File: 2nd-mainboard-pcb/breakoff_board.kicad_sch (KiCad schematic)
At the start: 28 parts, among them J13 ISP, J14 Spannungsmessung, J7 Quartz

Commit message: added libraries
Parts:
- added TP20: Quartz_2, symbol Connector:TestPoint
- TP1: value TestPoint -> Quartz_1
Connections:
- net Quartz_1: now also TP1.1
- net Quartz_2: now also TP20.1
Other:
- note added: "ADC-Messungen"
- note added: "Quartzmessung: Oszilloskop-Testpoints"
- note removed: "JTAG und ADC-Messungen Joint Test Action Group: standardisierte Schnittstelle für das Debugging und Testen von Mikrocontrollern"
- note removed: "Quartzmessung"
- note removed: "TDI (Test Data In) PC2 TDO (Test Data Out) PC3 TMS (Test Mode Select) PC4 TCK (Test Clock) PC5"
- moved on the sheet: J7, R14, R15, R16, TP1, TP14, TP15, TP16, TP17, TP7, TP8

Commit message: finished stacked design, annotaded
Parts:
- removed J14: Spannungsmessung, symbol Connector:Conn_01x05_Socket
- removed R16: 0.1, symbol Device:R
- removed TP16: I_Sense_12V_P, symbol Connector:TestPoint_Probe
- added J17: Spannungsmessung, symbol Connector:Conn_01x06_Socket
- added R23, R24: 0.1, symbol Device:R
- added TP13: I_Sense_12V_P, symbol Connector:TestPoint_Probe
- added TP14: I_Sense_12V_N, symbol Connector:TestPoint_Probe
- added TP7: I_Sense_5V_POW_P, symbol Connector:TestPoint_Probe
- added TP8: I_Sense_5V_POW_N, symbol Connector:TestPoint_Probe
- added TP9: I_Sense_5V, symbol Connector:TestPoint_2Pole
- TP17: value I_Sense_12V_N -> Netzteil_Test; footprint (none) -> TestPoint:TestPoint_Pad_D3.0mm
- TP5: renamed from TP14; value I_Sense_5V_P -> I_Sense_5V_USBC_P
- TP6: renamed from TP15; value I_Sense_5V_N -> I_Sense_5V_USBC_N
- renumbered D7 to D6, J13 to J18, J7 to J19, R17 to R20, R14 to R21, R15 to R22, R19 to R25, TP7 to TP1, TP19 to TP10, TP4 to TP11, TP2 to TP12, TP3 to TP15, TP5 to TP16, TP9 to TP18, TP12 to TP19, TP8 to TP2, TP13 to TP20, TP1 to TP21, TP11 to TP22, TP20 to TP23, TP10 to TP24, TP18 to TP3, TP6 to TP4
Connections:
- net +12V: now also J17.4 (Pin_4), R24.1, TP13.1
- net +3V3: now also J17.1 (Pin_1)
- net +5V: now also J17.2 (Pin_2), TP9.1; no longer R22.1, TP5.1
- net GND: now also J17.3 (Pin_3), R23.2, R24.2, TP14.1, TP8.1, TP9.2; no longer TP17.1
- net GND2: now also J17.6 (Pin_6)
- new net +24V: J17.5 (Pin_5), TP17.1
- new net +5V_POW: R23.1, TP7.1
- new net +5V_USBC: R22.1, TP5.1
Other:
- moved on the sheet: D6, J18, J19, R20, R21, R22, R25, TP1, TP10, TP11, TP12, TP15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

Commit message: alle bauteile hinzugefügt
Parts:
- removed J17: Spannungsmessung, symbol Connector:Conn_01x06_Socket
- removed J18: ISP, symbol Connector_Generic:Conn_02x03_Odd_Even
- added J21: ISP, Imported_Component_Footprints:FTSH-103-01-L-DH, symbol Imported_Component_Symbols:FTSH-103-01-L-DH
- added J22: Spannungsmessung, Connector_PinSocket_2.54mm:PinSocket_1x07_P2.54mm_Vertical, symbol Connector:Conn_01x07_Socket
- added TP7: 5V_POW_Test, TestPoint:TestPoint_Pad_D3.0mm, symbol Connector:TestPoint_Probe
- J23: renamed from J19; footprint (none) -> Connector_PinSocket_2.54mm:PinSocket_1x02_P2.54mm_Vertical
- R19: renamed from R25; footprint (none) -> Resistor_SMD:R_0402_1005Metric
- R20: renamed from R21; footprint (none) -> Resistor_SMD:R_0402_1005Metric
- R21: renamed from R22; footprint (none) -> Resistor_SMD:R_0402_1005Metric
- R22: renamed from R23; footprint (none) -> Resistor_SMD:R_0402_1005Metric
- R23: renamed from R24; footprint (none) -> Resistor_SMD:R_0402_1005Metric
- TP10: renamed from TP1; footprint (none) -> TestPoint:TestPoint_Pad_D2.0mm
- TP11: renamed from TP5; footprint (none) -> TestPoint:TestPoint_Pad_D2.0mm
- TP12: renamed from TP7; footprint (none) -> TestPoint:TestPoint_Pad_D2.0mm
- TP13: footprint (none) -> TestPoint:TestPoint_Pad_D2.0mm
- TP14: renamed from TP2; footprint (none) -> TestPoint:TestPoint_Pad_D2.0mm
- TP15: renamed from TP6; footprint (none) -> TestPoint:TestPoint_Pad_D2.0mm
- TP16: renamed from TP8; footprint (none) -> TestPoint:TestPoint_Pad_D2.0mm
- TP17: renamed from TP14; footprint (none) -> TestPoint:TestPoint_Pad_D2.0mm
- TP18: renamed from TP19; footprint (none) -> TestPoint:TestPoint_Pad_D2.0mm
- TP19: renamed from TP20; footprint (none) -> TestPoint:TestPoint_Pad_D2.0mm
- TP20: renamed from TP22; footprint (none) -> TestPoint:TestPoint_Pad_D2.0mm
- TP21: renamed from TP24; footprint (none) -> TestPoint:TestPoint_Pad_D2.0mm
- TP22: renamed from TP3; footprint (none) -> TestPoint:TestPoint_2Pads_Pitch2.54mm_Drill0.8mm
- TP23: renamed from TP9; footprint (none) -> TestPoint:TestPoint_2Pads_Pitch2.54mm_Drill0.8mm
- TP24: renamed from TP4; footprint (none) -> TestPoint:TestPoint_2Pads_Pitch2.54mm_Drill0.8mm
- TP25: renamed from TP10; footprint (none) -> TestPoint:TestPoint_2Pads_Pitch2.54mm_Drill0.8mm
- TP5: renamed from TP18; footprint (none) -> TestPoint:TestPoint_Pad_D2.0mm
- TP6: renamed from TP12; value 5V_Test -> 5V_USBC_Test
- TP8: renamed from TP21; footprint (none) -> TestPoint:TestPoint_Loop_D3.80mm_Drill2.5mm
- TP9: renamed from TP23; footprint (none) -> TestPoint:TestPoint_Loop_D3.80mm_Drill2.5mm
- renumbered D6 to D5, R20 to R18, TP11 to TP1, TP15 to TP2, TP16 to TP3, TP17 to TP4
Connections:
- net +12V: now also J22.5 (Pin_5)
- net +24V: now also J22.6 (Pin_6)
- net +3V3: now also J22.1 (Pin_1)
- net +5V_POW: now also D5.2 (A), R19.1, TP23.1, J21.02, J22.3 (Pin_3), TP7.1
- net +5V_USBC: now also TP22.1, TP6.1, J22.2 (Pin_2)
- net GND: now also J21.06, J22.4 (Pin_4)
- net GND2: now also J22.7 (Pin_7)
- net MISO: now also J21.01
- net MOSI: now also J21.04
- net RESET: now also J21.05
- net SCK: now also J21.03
- removed net +5V: D5.2 (A), R19.1, TP22.1, TP23.1, TP6.1
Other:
- moved on the sheet: TP1, TP2, TP3, TP4, TP5, TP6

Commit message: Fan-PCB-Beginning
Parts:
- removed J21: ISP, Imported_Component_Footprints:FTSH-103-01-L-DH, symbol Imported_Component_Symbols:FTSH-103-01-L-DH
- added J16: ISP, Connector_PinHeader_2.54mm:PinHeader_2x03_P2.54mm_Vertical, symbol Connector_Generic:Conn_02x03_Odd_Even
- renumbered D5 to D7, J22 to J17, J23 to J18, R18 to R16, R19 to R17, R20 to R18, R21 to R19, R22 to R20, R23 to R21
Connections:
- net +5V_POW: now also J16.2 (Pin_2)
- net GND: now also J16.6 (Pin_6)
- net MISO: now also J16.1 (Pin_1)
- net MOSI: now also J16.4 (Pin_4)
- net RESET: now also J16.5 (Pin_5)
- net SCK: now also J16.3 (Pin_3)

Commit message: Testpoints hinzugefügt
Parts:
- removed J17: Spannungsmessung, Connector_PinSocket_2.54mm:PinSocket_1x07_P2.54mm_Vertical, symbol Connector:Conn_01x07_Socket
- removed R18, R19, R20, R21: 0.1, Resistor_SMD:R_0402_1005Metric, symbol Device:R
- removed TP1: 3V3_Test, TestPoint:TestPoint_Pad_D3.0mm, symbol Connector:TestPoint_Probe
- removed TP10: I_Sense_3V3_P, TestPoint:TestPoint_Pad_D2.0mm, symbol Connector:TestPoint_Probe
- removed TP11: I_Sense_5V_USBC_P, TestPoint:TestPoint_Pad_D2.0mm, symbol Connector:TestPoint_Probe
- removed TP12: I_Sense_5V_POW_P, TestPoint:TestPoint_Pad_D2.0mm, symbol Connector:TestPoint_Probe
- removed TP13: I_Sense_12V_P, TestPoint:TestPoint_Pad_D2.0mm, symbol Connector:TestPoint_Probe
- removed TP14: I_Sense_3V3_N, TestPoint:TestPoint_Pad_D2.0mm, symbol Connector:TestPoint_Probe
- removed TP15: I_Sense_5V_USBC_N, TestPoint:TestPoint_Pad_D2.0mm, symbol Connector:TestPoint_Probe
- removed TP16: I_Sense_5V_POW_N, TestPoint:TestPoint_Pad_D2.0mm, symbol Connector:TestPoint_Probe
- removed TP17: I_Sense_12V_N, TestPoint:TestPoint_Pad_D2.0mm, symbol Connector:TestPoint_Probe
- removed TP24: I_Sense_3V3, TestPoint:TestPoint_2Pads_Pitch2.54mm_Drill0.8mm, symbol Connector:TestPoint_2Pole
- removed TP4: Netzteil_Test, TestPoint:TestPoint_Pad_D3.0mm, symbol Connector:TestPoint_Probe
- removed TP5: GND_12V_Test, TestPoint:TestPoint_Pad_D2.0mm, symbol Connector:TestPoint_Probe
- added J23: Conn_01x04_Socket, Connector_PinSocket_2.54mm:PinSocket_1x04_P2.54mm_Vertical, symbol Connector:Conn_01x04_Socket
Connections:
- net +12V: now also J23.4 (Pin_4)
- net +5V_POW: now also J23.2 (Pin_2)
- net +5V_USBC: now also J23.1 (Pin_1)
- net GND: now also J23.3 (Pin_3)
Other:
- note added: "Strommessung"
- note removed: "Direkte Strommessung"
- note removed: "Shunt-Widerstand"
- note removed: "Strommessung mit Spannungsmessung"
- moved on the sheet: TP22, TP23, TP25

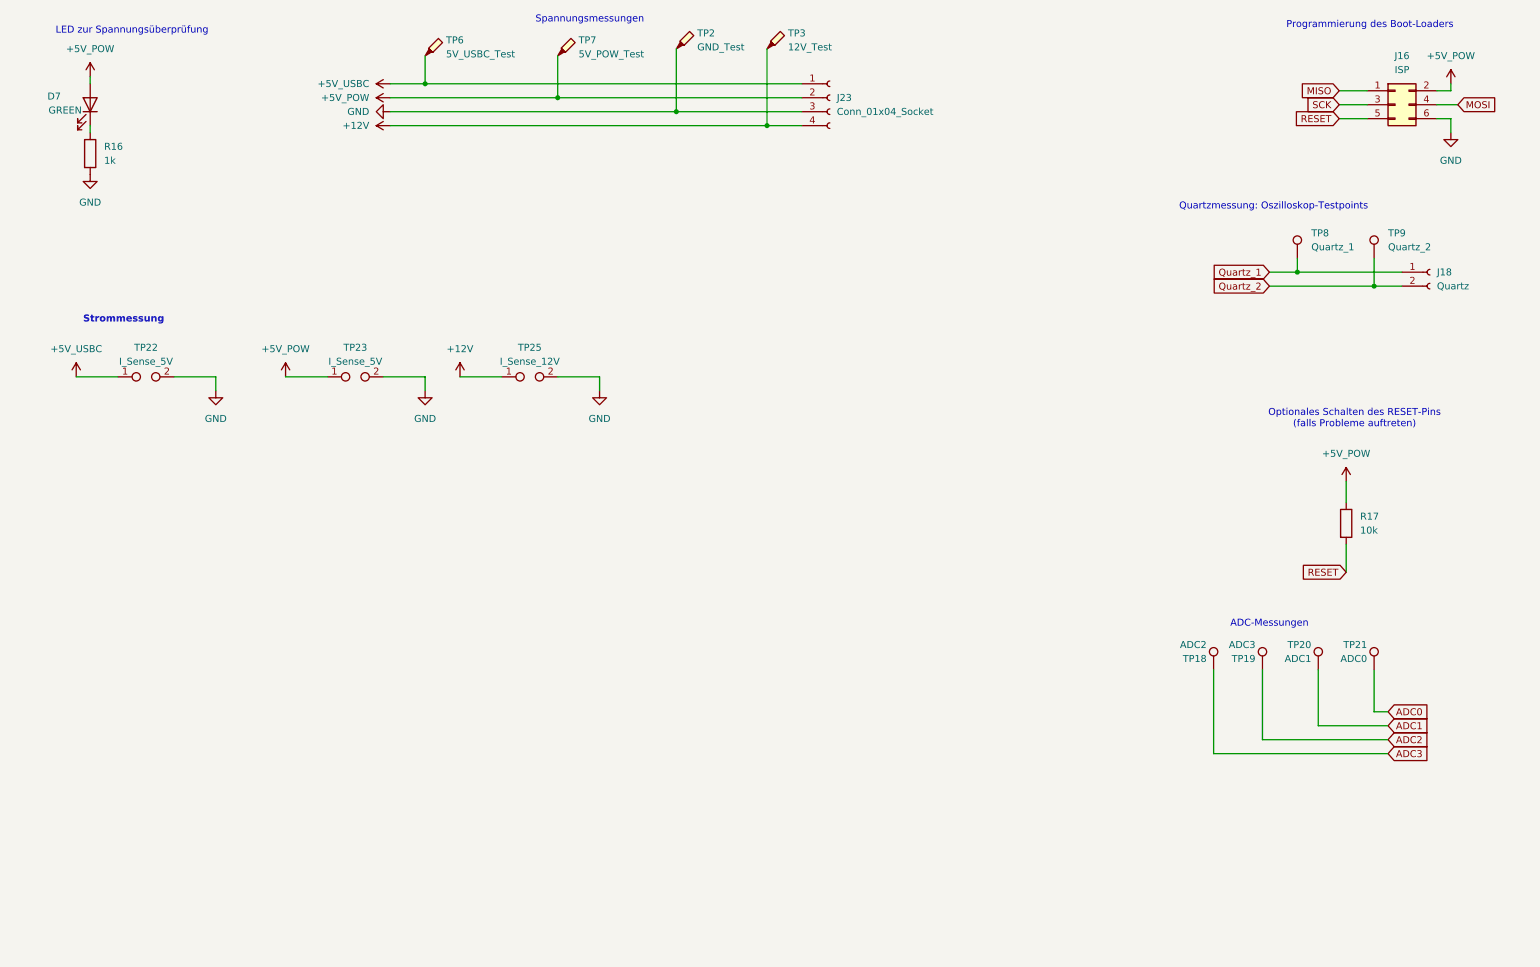
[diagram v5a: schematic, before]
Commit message: updated a bit of the track widths, removed comments in schematic
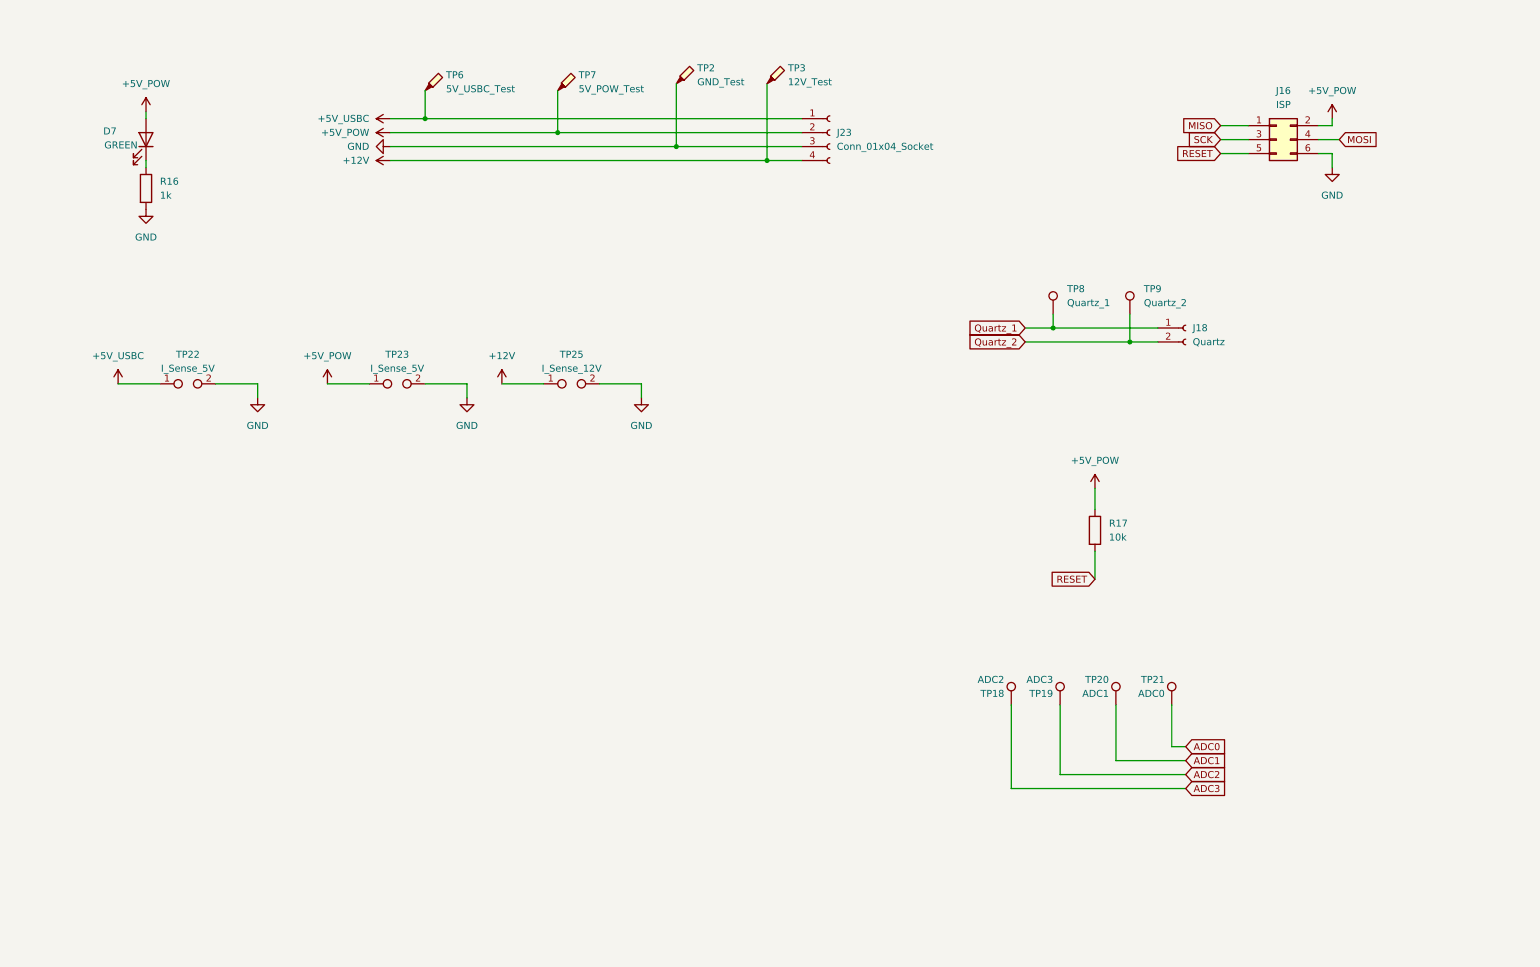
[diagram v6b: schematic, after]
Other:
- note removed: "ADC-Messungen"
- note removed: "LED zur Spannungsüberprüfung"
- note removed: "Optionales Schalten des RESET-Pins (falls Probleme auftreten)"
- note removed: "Programmierung des Boot-Loaders"
- note removed: "Quartzmessung: Oszilloskop-Testpoints"
- note removed: "Spannungsmessungen"
- note removed: "Strommessung"
- moved on the sheet: D7, J16, J18, J23, R16, R17, TP18, TP19, TP2, TP20, TP21, TP22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

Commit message: stacked pcb reworked
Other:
- moved on the sheet: D7, R16
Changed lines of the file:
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@@
 	(wire
 		(pts
-			(xy 35.56 33.02) (xy 35.56 34.29)
+			(xy 35.56 27.94) (xy 35.56 29.21)
 		)
 		(stroke
@@
 	(wire
 		(pts
-			(xy 35.56 41.91) (xy 35.56 43.18)
+			(xy 35.56 36.83) (xy 35.56 38.1)
 		)
 		(stroke
@@
 	(symbol
 		(lib_id "power:+5VP")
-		(at 35.56 33.02 0)
+		(at 35.56 27.94 0)
 		(unit 1)
 		(exclude_from_sim no)
@@
 		(fields_autoplaced yes)
 		(property "Reference" "#PWR088"
-			(at 35.56 36.83 0)
+			(at 35.56 31.75 0)
 			(effects
 				(font
@@
 		)
 		(property "Value" "+5V_POW"
+			(at 35.56 22.86 0)
+			(effects
+				(font
+					(size 1.27 1.27)
+				)
+			)
+		)
+		(property "Footprint" ""
 			(at 35.56 27.94 0)
 			(effects
@@
 					(size 1.27 1.27)
 				)
-			)
-		)
-		(property "Footprint" ""
-			(at 35.56 33.02 0)
-			(effects
-				(font
-					(size 1.27 1.27)
-				)
 				(hide yes)
 			)
 		)
 		(property "Datasheet" ""
-			(at 35.56 33.02 0)
+			(at 35.56 27.94 0)
 			(effects
 				(font
@@
 		)
 		(property "Description" "Power symbol creates a global label with name \"+5VP\""
-			(at 35.56 33.02 0)
+			(at 35.56 27.94 0)
 			(effects
 				(font
@@
 	(symbol
 		(lib_id "power:GND")
-		(at 35.56 50.8 0)
+		(at 35.56 45.72 0)
 		(unit 1)
 		(exclude_from_sim no)
@@
 		(fields_autoplaced yes)
 		(property "Reference" "#PWR097"
-			(at 35.56 57.15 0)
+			(at 35.56 52.07 0)
 			(effects
 				(font
@@
 		)
 		(property "Value" "GND"
-			(at 35.56 55.88 0)
+			(at 35.56 50.8 0)
 			(effects
 				(font
@@
 		)
 		(property "Footprint" ""
-			(at 35.56 50.8 0)
+			(at 35.56 45.72 0)
 			(effects
 				(font
@@
 		)
 		(property "Datasheet" ""
-			(at 35.56 50.8 0)
+			(at 35.56 45.72 0)
 			(effects
 				(font
@@
 		)
 		(property "Description" "Power symbol creates a global label with name \"GND\" , ground"
-			(at 35.56 50.8 0)
+			(at 35.56 45.72 0)
 			(effects
 				(font
@@
 	(symbol
 		(lib_id "Device:LED")
-		(at 35.56 38.1 270)
+		(at 35.56 33.02 270)
 		(mirror x)
 		(unit 1)
@@
 		(dnp no)
 		(property "Reference" "D7"
-			(at 30.226 36.576 90)
+			(at 30.226 31.496 90)
 			(effects
 				(font
@@
 		)
 		(property "Value" "GREEN"
-			(at 34.036 39.116 90)
+			(at 34.036 34.036 90)
 			(effects
 				(font
@@
 		)
 		(property "Footprint" "LED_SMD:LED_0805_2012Metric"
-			(at 35.56 38.1 0)
+			(at 35.56 33.02 0)
 			(effects
 				(font
@@
 		)
 		(property "Datasheet" "~"
-			(at 35.56 38.1 0)
+			(at 35.56 33.02 0)
 			(effects
 				(font
@@
 		)
 		(property "Description" "Light emitting diode"
-			(at 35.56 38.1 0)
+			(at 35.56 33.02 0)
 			(effects
 				(font
@@
 	(symbol
 		(lib_id "Device:R")
-		(at 35.56 46.99 0)
+		(at 35.56 41.91 0)
 		(unit 1)
 		(exclude_from_sim no)
@@
 		(fields_autoplaced yes)
 		(property "Reference" "R16"
-			(at 38.1 45.7199 0)
+			(at 38.1 40.6399 0)
 			(effects
 				(font
@@
 		)
 		(property "Value" "1k"
-			(at 38.1 48.2599 0)
+			(at 38.1 43.1799 0)
 			(effects
 				(font
@@
 		)
 		(property "Footprint" "Resistor_SMD:R_0402_1005Metric"
-			(at 33.782 46.99 90)
+			(at 33.782 41.91 90)
 			(effects
 				(font
@@
 		)
 		(property "Datasheet" "~"
-			(at 35.56 46.99 0)
+			(at 35.56 41.91 0)
 			(effects
 				(font
@@
 		)
 		(property "Description" "Resistor"
-			(at 35.56 46.99 0)
-			(effects
-				(font
+			(at 35.56 41.91 0)
+			(effects
+				(font
